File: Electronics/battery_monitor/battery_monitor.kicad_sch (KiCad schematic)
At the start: 23 parts, among them IC1 MIC2779H-1YM5_TR, J2 Conn_01x02_Pin, J2 Conn_01x04_Male, J3 Conn_01x02_Pin, Q1 DMP4015SK3-13, Q4 BS170, U1 HT7533; LDI8233-05U, U2 INA226

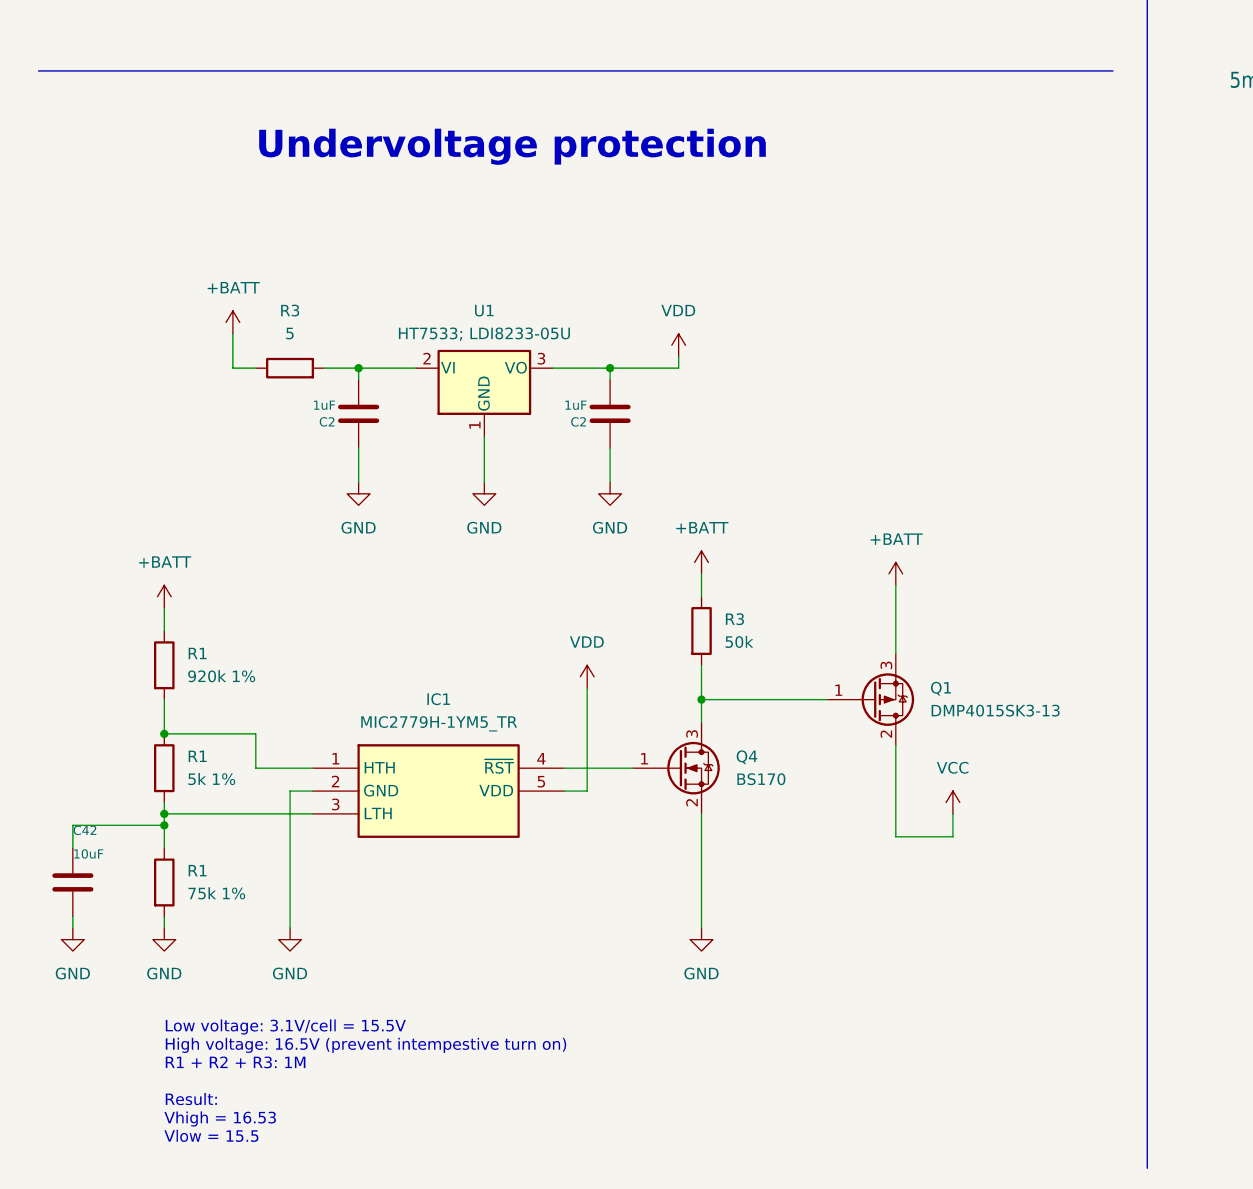
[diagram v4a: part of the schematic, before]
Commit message: Electronics: correction to battery_monitor PCB
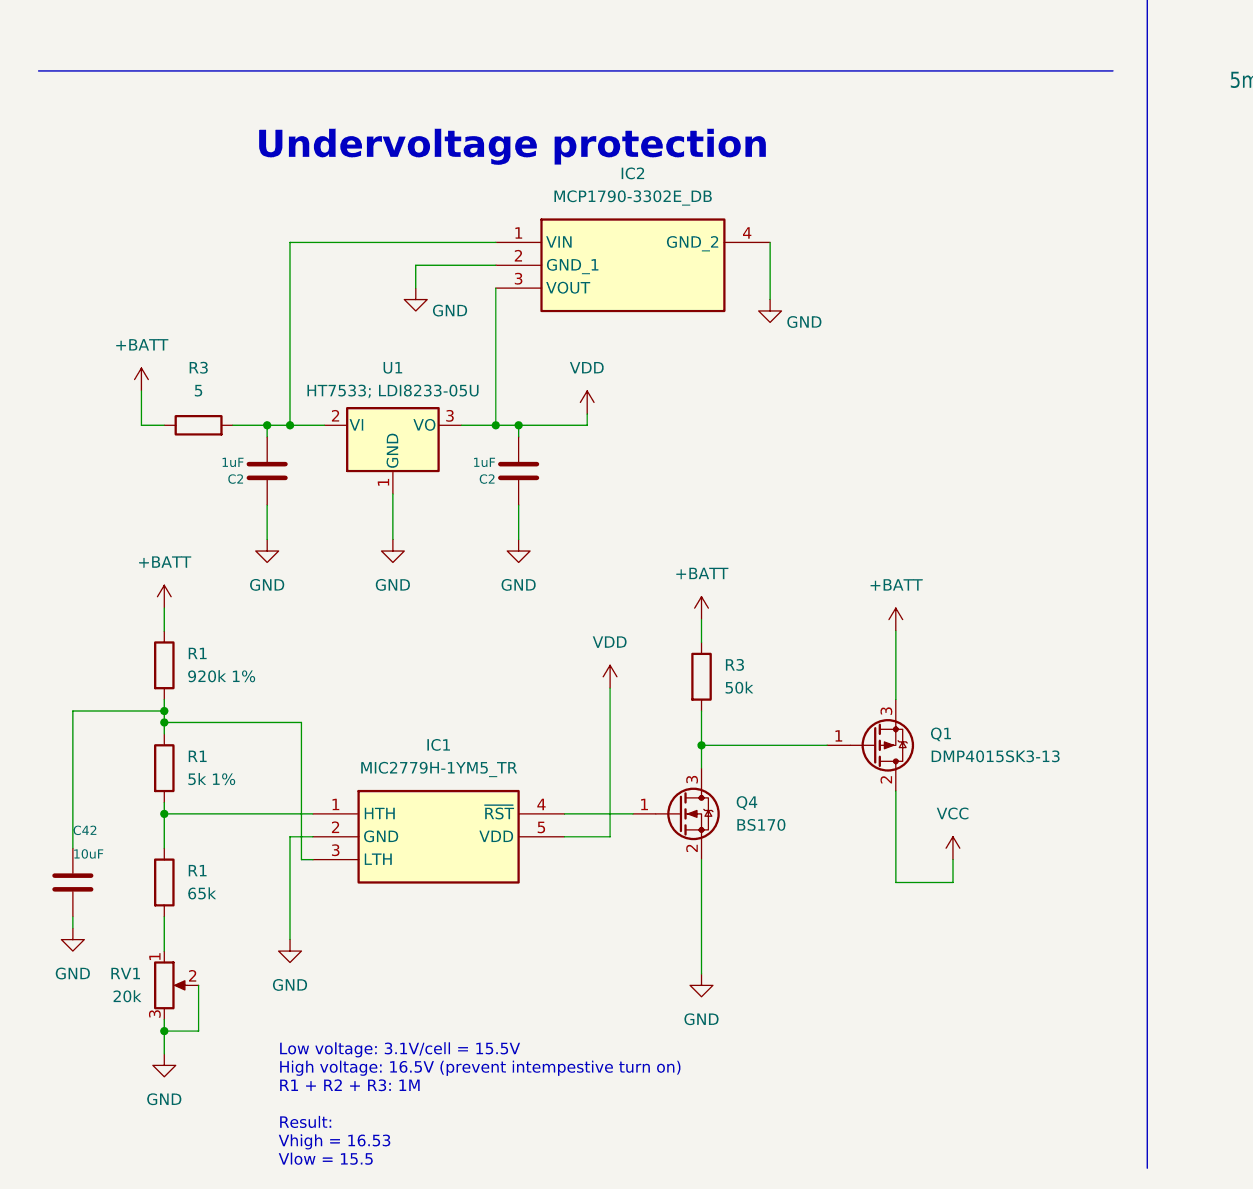
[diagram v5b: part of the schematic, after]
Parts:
- added IC2: MCP1790-3302E_DB, SOT230P700X180-4N, symbol MCP1790-3302E_DB:MCP1790-3302E_DB
- added RV1: 20k, Potentiometer_SMD:Potentiometer_Bourns_3314J_Vertical, symbol Device:R_Potentiometer
- R1: value 75k 1% -> 65k; Mouser Part Number 603-RC0805FR-0775KL -> 708-6676
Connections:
- net GND: now also IC2.2 (GND_1), IC2.4 (GND_2), RV1.2, RV1.3; no longer R1.2
- net VDD: now also IC2.3 (VOUT)
- net at C2.2, R3.2, U1.2 (VI): now also IC2.1 (VIN)
- net at R1.1, R1.2: now also C42.1, IC1.3 (LTH); no longer IC1.1 (HTH)
- net at R1.1, R1.2: now also IC1.1 (HTH); no longer C42.1, IC1.3 (LTH)
- new net: R1.2, RV1.1
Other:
- moved on the sheet: C2, IC1, Q1, Q4, R3, U1

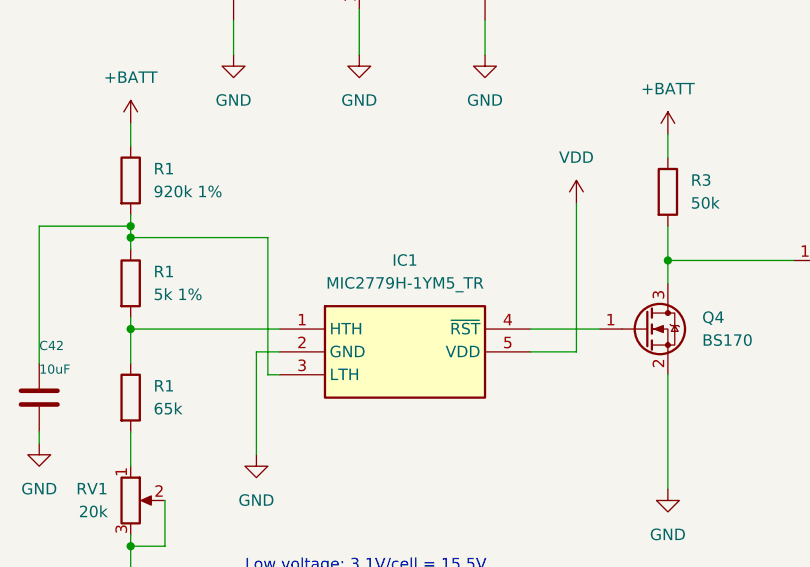
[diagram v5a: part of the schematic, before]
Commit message: Fix bug in init phase ; swap right/left motor after hardware change.
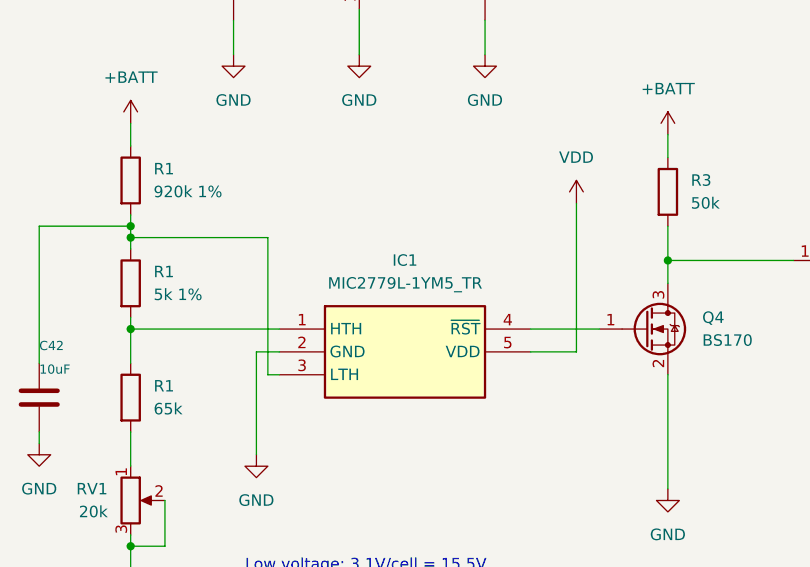
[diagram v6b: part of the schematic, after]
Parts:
- IC1: value MIC2779H-1YM5_TR -> MIC2779L-1YM5_TR
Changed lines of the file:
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@@
       (effects (font (size 1.27 1.27)))
     )
-    (property "Value" "MIC2779H-1YM5_TR" (at 59.69 149.86 0)
+    (property "Value" "MIC2779L-1YM5_TR" (at 59.69 149.86 0)
       (effects (font (size 1.27 1.27)))
     )
